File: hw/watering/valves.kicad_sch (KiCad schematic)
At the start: 2 parts, among them J1 Conn_01x02_Pin, U2 AL8860WT

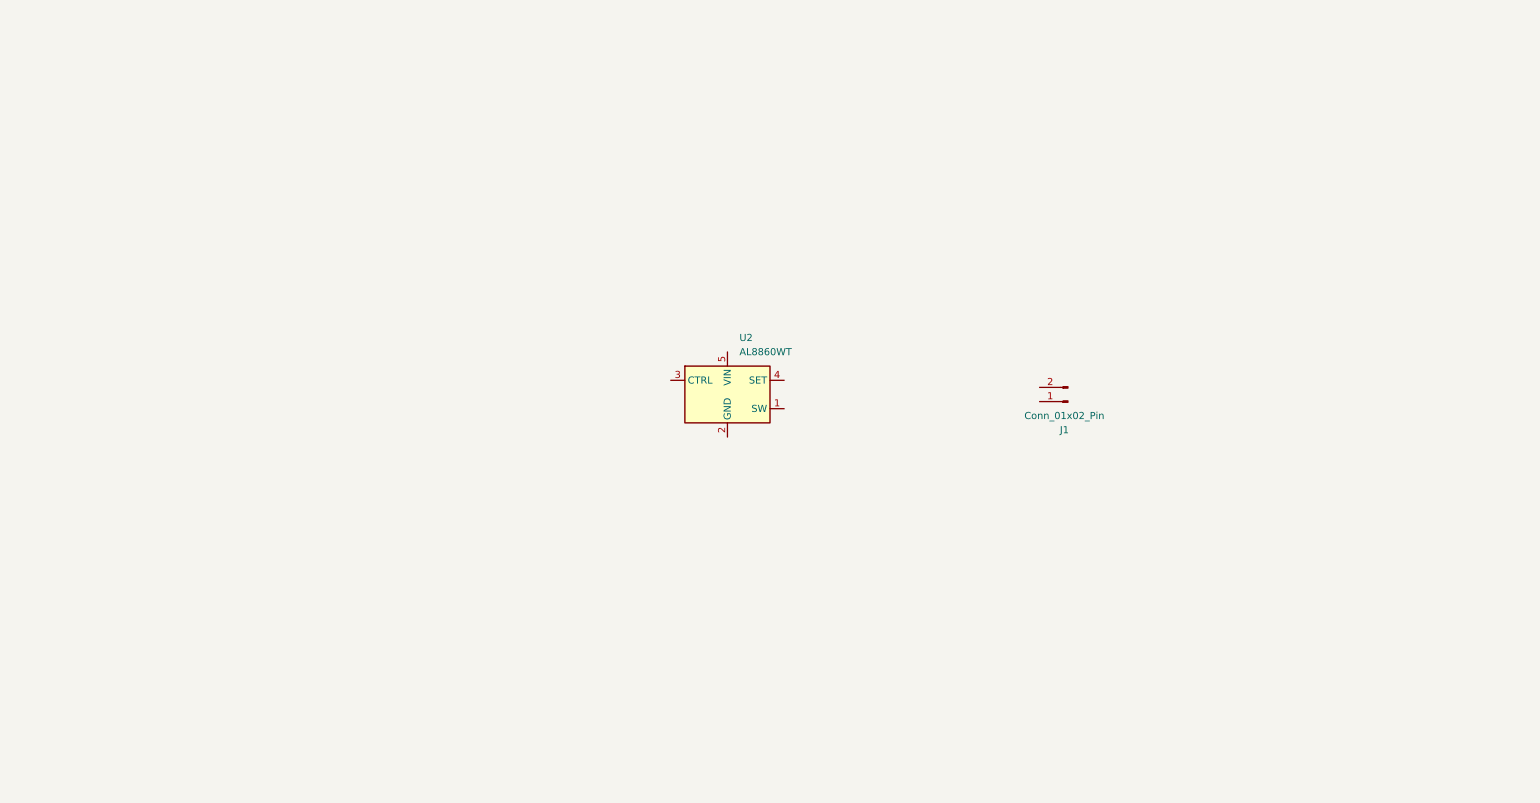
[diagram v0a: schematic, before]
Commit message: added battery management chip
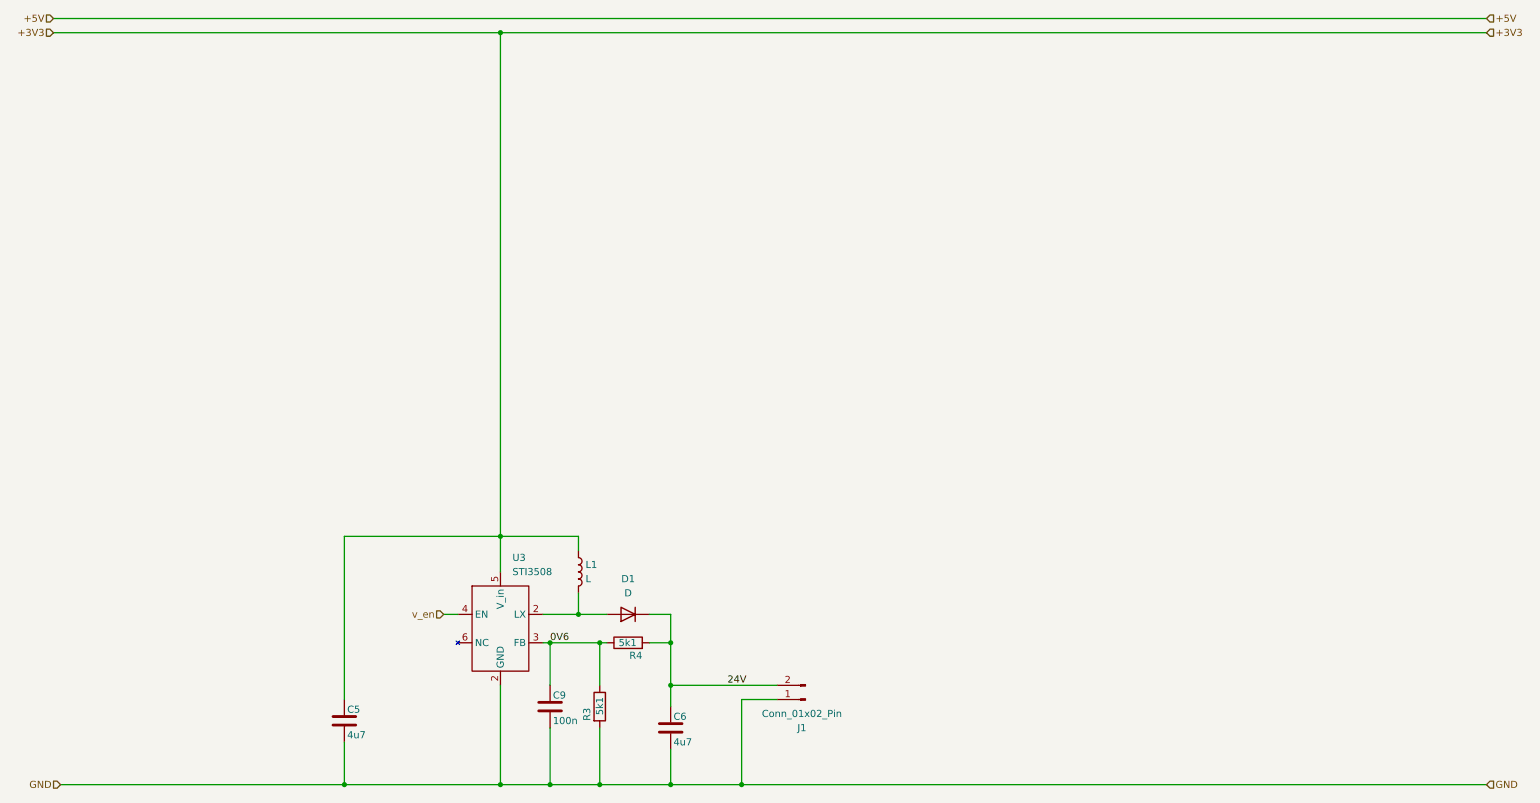
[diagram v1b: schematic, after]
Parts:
- removed U2: AL8860WT, Package_TO_SOT_SMD:TSOT-23-5, symbol Driver_LED:AL8860WT
- added C5, C6: 4u7, Capacitor_SMD:C_0603_1608Metric, symbol Device:C
- added C9: 100n, Capacitor_SMD:C_0603_1608Metric, symbol Device:C
- added D1: D, symbol Device:D
- added L1: L, symbol Device:L
- added R3, R4: 5k1, Resistor_SMD:R_0603_1608Metric, symbol Device:R
- added U3: STI3508, Package_TO_SOT_SMD:SOT-23-6, symbol sti3508:STI3508
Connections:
- net GND: now reaches J1.1 (Pin_1)
- net GND: now also C5.2, C6.2, C9.2, R3.2, U3.2 (LX)
- net 24V: now reaches J1.2 (Pin_2)
- net 24V: now also C6.1, D1.1 (K), R4.2
- new net: D1.2 (A), L1.2, U3.2 (LX)
- new net +3V3: C5.1, L1.1, U3.5 (V_in)
- new net 0V6: C9.1, R3.1, R4.1, U3.3 (FB)
- new net v_en: U3.4 (EN)
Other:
- moved on the sheet: J1

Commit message: updated power
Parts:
- removed C5, C6: 4u7, Capacitor_SMD:C_0603_1608Metric, symbol Device:C
- removed C9: 100n, Capacitor_SMD:C_0603_1608Metric, symbol Device:C
- removed D1: D, symbol Device:D
- removed L1: L, symbol Device:L
- added C29, C33: 22u, Capacitor_SMD:C_1206_3216Metric, symbol Device:C
- added D6: SS210, Diode_SMD:D_SMA, symbol Device:D
- added L5: 22u, Inductor_SMD:L_Wuerth_MAPI-4030, symbol Device:L
- R12: renamed from R3; value 5k1 -> 1k
- R13: renamed from R4; value 5k1 -> 39k
- renumbered J1 to J4, U3 to U6
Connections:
- net +3V3: now also C29.1, L5.1
- net 24V: now also C33.1, D6.1 (K)
- net GND: now also C29.2, C33.2
- new net: D6.2 (A), L5.2, U6.2 (LX)

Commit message: hardware progres
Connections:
- net at D6.2 (A), L5.2: now also U6.1 (LX); no longer U6.2 (LX)
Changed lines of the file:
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@@
 		(pin "3"
 		)
-		(pin "2"
+		(pin "1"
 		)
 		(instances
@@
 			)
 		)
-		(property "Datasheet" ""
+		(property "Datasheet" "https://jlc-prod-smt.oss-eu-central-1.aliyuncs.com/smtDataManualFile/8579706240215273472-C23153.pdf?response-content-disposition=attachment%3B%20filename%3DC23153.pdf%3B%20filename%2A%3DUTF-8%27%27C23153.pdf&x-oss-date=20260604T212837Z&x-oss-expires=1800&x-oss-security-token=CAISgAN1q6Ft5B2yfSjIr5qGBvnBmah58ZCnSW2IvnU%2FOOZNta3duzz2IHhMdHJsAOodtv0%2FmmhT6PkclqRLcbhpcmfjV%2BZHzLB8qc9%2FokVA4J7b16cNrbH4M4H6aXeirtuwDsz9SNTCALjPD3nPii50x5bjaDymRCbLGJaViJlhHLN1Ow6jdmhpCctxLAlvo9NgFxm3D%2Fu2NQPwiWf9FVdhvhEG6Vly8qOi2MaRmFy8yFTx0b0SvJ%2BjYMrmPctoN9JnSdC5mfdzau3a1TJ84gRD0a5wkaVA1zbDs5bfISEIuUzebreLqY03dV4mOvdqIcMe8qigz88fk%2FfIioH6xyxKOexoSCnFTOiiupCcQLPyao9jLu6iayqViY7QaIOTqQohZmkAMwVOasAsI3Ngh4zF97Qt0cVNkXO9gWfLI8DtuMleWqrvQN5iAnSgc5lCkRRYwGs1287ugXlSQzo890KPDAEovaKCnZ2ZSfh7Y4sNknI6i%2Bfc2Se2MIkILjrImKKWD5sagAFp6e2CTF5gXCAetl%2FZznzBeiqXvbdtrNp24XwBckBwOk4pCo9PLwSFMgOtQSf5U6kP%2F%2Bd1fI%2BKr022AwW2hsiCSfA6ItkAjrYqmnkpM1k6ce1E8ls7kKfeT%2Fq%2FikPDk77ij56kdNpXvKHTlexuI%2FHtV9DEGaEJEWVb894cTL2j2iAA&x-oss-signature-version=OSS4-HMAC-SHA256&x-oss-credential=STS.NY3MCutwXFRLKK9Zuj4iaZhvY%2F20260604%2Feu-central-1%2Foss%2Faliyun_v4_request&x-oss-signature=50b712f2b003cbfdc0278338a33b0530e7203f95c21e53b9561c1751bbef5ab5"
 			(at 123.19 133.35 0)
 			(hide yes)
@@
 			)
 		)
-		(property "Description" "Resistor"
+		(property "Description" "C23153"
 			(at 123.19 133.35 0)
 			(hide yes)
@@
 			)
 		)
-		(property "Datasheet" ""
+		(property "Datasheet" "https://jlc-prod-smt.oss-eu-central-1.aliyuncs.com/smtDataManualFile/8579706098724622336-C21190.pdf?response-content-disposition=attachment%3B%20filename%3DC21190.pdf%3B%20filename%2A%3DUTF-8%27%27C21190.pdf&x-oss-date=20260604T201055Z&x-oss-expires=1800&x-oss-security-token=CAISgAN1q6Ft5B2yfSjIr5rnDe%2F5h6h02fGfW1HcsFYmaelfp6rpszz2IHhMdHJsAOodtv0%2FmmhT6PkclqRLcbhpcmfjV%2BZHzLB8qeACnUZA4J7b16cNrbH4M4H6aXeirtuwDsz9SNTCALjPD3nPii50x5bjaDymRCbLGJaViJlhHLN1Ow6jdmhpCctxLAlvo9NgFxm3D%2Fu2NQPwiWf9FVdhvhEG6Vly8qOi2MaRmFy8yFTx0b0SvJ%2BjYMrmPctoN9JnSdC5mfdzau3a1TJ84gRD0a5wkaVA1zbDs5bfISEIuUzebreLqY03dV4mOvdqIcMe8qigz88fk%2FfIioH6xyxKOexoSCnFTOiiupCcQLPyao9jLu6iayqViY7QaIOTqQohZmkAMwVOasAsI3Ngh4zF97Qt0cVNkXO9gWfLI8DtuMleWhqD30JB3tHD0eS19jklBdzSlusJRAJJUVBflCeKEaRNSAd3WGhEfM2%2BBt4QT30w5N2u00S8OSMIc%2BkdiqKWD5sagAFWQNkecW6D1E4coUzPadT7SCc3f42V3X5rSfMFH84ElX%2BTmNGNYscgqDx0xyaTJyyrM%2BFQW4w%2FhWX4qrYQWwgwoGw%2BQzNTMlILHbcsYIbLhGAndRWnhNlBy%2F%2FsrfRbXWVyCjftSb4xwrnr%2BixQsq7hkcXqmYOc23lG%2B0BooZpCuSAA&x-oss-signature-version=OSS4-HMAC-SHA256&x-oss-credential=STS.NYRFUMjwUn3tYwmTVsefsHoBQ%2F20260604%2Feu-central-1%2Foss%2Faliyun_v4_request&x-oss-signature=c8ef4b7bb2f46d5880b5f7d119351002df83d06270cd391a72e44158b7fb7248"
 			(at 118.11 144.78 0)
 			(hide yes)
@@
 			)
 		)
-		(property "Description" "Resistor"
+		(property "Description" "C21190"
 			(at 118.11 144.78 0)
 			(hide yes)

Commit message: routing done
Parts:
- J4: footprint (none) -> DORABO:DB142R-5.08-2P-GN
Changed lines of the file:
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@@
 			)
 		)
-		(property "Footprint" ""
+		(property "Footprint" "DORABO:DB142R-5.08-2P-GN"
 			(at 154.94 143.51 0)
 			(hide yes)
@@
 			)
 		)
-		(property "Datasheet" ""
+		(property "Datasheet" "https://jlc-prod-smt.oss-eu-central-1.aliyuncs.com/smtDataManualFile/8588944103362990080-C2898709.pdf?response-content-disposition=attachment%3B%20filename%3DC2898709.pdf%3B%20filename%2A%3DUTF-8%27%27C2898709.pdf&x-oss-date=20260610T103254Z&x-oss-expires=1800&x-oss-security-token=CAISgAN1q6Ft5B2yfSjIr5rzGerOqIdH2oOoclzHiVFsdbhe1vCYszz2IHhMdHJsAOodtv0%2FmmhT6PkclqRLcbhpcmfjV%2BZHzLB8qdNq3GlC4J7b16cNrbH4M4H6aXeirtuwDsz9SNTCALjPD3nPii50x5bjaDymRCbLGJaViJlhHLN1Ow6jdmhpCctxLAlvo9NgFxm3D%2Fu2NQPwiWf9FVdhvhEG6Vly8qOi2MaRmFy8yFTx0b0SvJ%2BjYMrmPctoN9JnSdC5mfdzau3a1TJ84gRD0a5wkaVA1zbDs5bfISEIuUzebreLqY03dV4mOvdqIcMe8qigz88fk%2FfIioH6xyxKOexoSCnFTOiiupCcQLPyao9jLu6iayqViY7QaIOTqQohZmkAMwVOasAsI3Ngh4zF97Qt0cVNkXO9gWfLI8DtuMleWirs1UNH%2FtHD0eS19jklBdzSlusJRAJJUVBflCeKEaRNSAd3WGhEfM2%2BBt4QT30w5N2u00S8OSMIsaRmZ6KWD5sagAEvGX7RQli9n0idv9ihEU8A%2Bbh5MIwx%2F6mEDEdw7rPt8GvYywCHHAO%2FvmfamD6hWJK1CjyEuU3UmXrstWZ7FJZiXCRquNSQNh07tVtxLzhRH4RSBWWrBck%2B00KmW9tmwnDDBERstBLHwgZAtDcvABP8phEVP1O0gWNEZDZaGHKiVSAA&x-oss-signature-version=OSS4-HMAC-SHA256&x-oss-credential=STS.NYFRPzEXfmACpzvmQ9y7r953Q%2F20260610%2Feu-central-1%2Foss%2Faliyun_v4_request&x-oss-signature=91314ede9ab8009bd2a96ac59210a76d2245a17ff8fcc2e7e63cd5e128038b30"
 			(at 154.94 143.51 0)
 			(hide yes)
@@
 			)
 		)
-		(property "Description" "Generic connector, single row, 01x02, script generated"
+		(property "Description" "C2898709"
 			(at 154.94 143.51 0)
 			(hide yes)

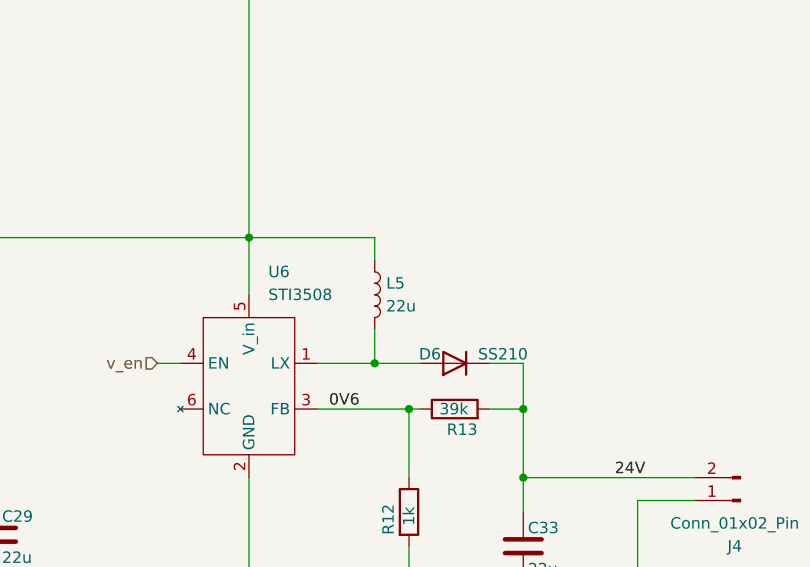
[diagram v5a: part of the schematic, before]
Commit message: updated inductors
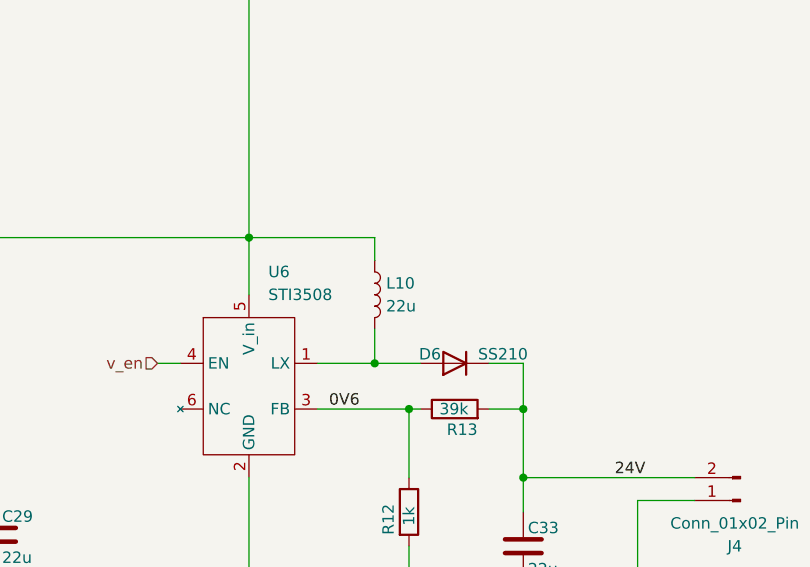
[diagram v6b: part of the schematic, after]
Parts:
- removed L5: 22u, Inductor_SMD:L_Wuerth_MAPI-4030, symbol Device:L
- added L10: 22u, Inductor_SMD:L_Changjiang_FTC303020D, symbol Device:L
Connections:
- net +3V3: now also L10.1
- net at D6.2 (A), U6.1 (LX): now also L10.2
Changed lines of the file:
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@@
+	)
+	(symbol
+		(lib_id "Device:L")
+		(at 114.3 120.65 0)
+		(unit 1)
+		(body_style 1)
+		(exclude_from_sim no)
+		(in_bom yes)
+		(on_board yes)
+		(in_pos_files yes)
+		(dnp no)
+		(fields_autoplaced yes)
+		(property "Reference" "L10"
+			(at 115.57 119.3799 0)
+			(show_name no)
+			(do_not_autoplace no)
+			(effects
+				(font
+					(size 1.27 1.27)
+				)
+				(justify left)
+			)
+		)
+		(property "Value" "22u"
+			(at 115.57 121.9199 0)
+			(show_name no)
+			(do_not_autoplace no)
+			(effects
+				(font
+					(size 1.27 1.27)
+				)
+				(justify left)
+			)
+		)
+		(property "Footprint" "Inductor_SMD:L_Changjiang_FTC303020D"
+			(at 114.3 120.65 0)
+			(hide yes)
+			(show_name no)
+			(do_not_autoplace no)
+			(effects
+				(font
+					(size 1.27 1.27)
+				)
+			)
+		)
+		(property "Datasheet" "https://jlc-prod-smt.oss-eu-central-1.aliyuncs.com/smtDataManualFile/8603011017442553856-C18724424.pdf?response-content-disposition=attachment%3B%20filename%3DC18724424.pdf%3B%20filename%2A%3DUTF-8%27%27C18724424.pdf&x-oss-date=20260615T131049Z&x-oss-expires=1800&x-oss-security-token=CAISgAN1q6Ft5B2yfSjIr5r7EvjHqrJS76GJWlCDrFA3esRehaLlqTz2IHhMdHJsAOodtv0%2FmmhT6PkclqRLcbhpcmfjV%2BZHzLB8qbYvhD9F4J7b16cNrbH4M4H6aXeirtuwDsz9SNTCALjPD3nPii50x5bjaDymRCbLGJaViJlhHLN1Ow6jdmhpCctxLAlvo9NgFxm3D%2Fu2NQPwiWf9FVdhvhEG6Vly8qOi2MaRmFy8yFTx0b0SvJ%2BjYMrmPctoN9JnSdC5mfdzau3a1TJ84gRD0a5wkaVA1zbDs5bfISEIuUzebreLqY03dV4mOvdqIcMe8qigz88fk%2FfIioH6xyxKOexoSCnFTOiiupCcQLPyao9jLu6iayqViY7QaIOTqQohZmkAMwVOasAsI3Ngh4zF97Qt0cVNkXO9gWfLI8DtuMleWkqmQftNonSgc5lCkRRYwGs1287ugXlSQzo890KPDAEovaKCnZ2ZSfh7Y4sNknI6i%2Bfc2Se2MIkI78F9wqKWD5sagAGgIrBpqkaDNLB%2FeRrJRXX%2BUI0WHkJQELKIEfuONtPHcqXYkRDIHor0h8sEmAzdWEcuJqyAotIM3sYVhSK9RCw9rtluv0dJx48JCxsibZlIjb%2B0NEIprmvzFpJBKJEQoS2JBuBmZ0uKENGbbnHMTewPmke4yqImGUR1dELAyCJ5ASAA&x-oss-signature-version=OSS4-HMAC-SHA256&x-oss-credential=STS.NYNYBsGmsXcbXv2HPbvKrjgNK%2F20260615%2Feu-central-1%2Foss%2Faliyun_v4_request&x-oss-signature=9cbeeebf1f2dbb1e5d82ef5fe3da511c573dfc2eaeab7f382c23f43e5666c8af"
+			(at 114.3 120.65 0)
+			(hide yes)
+			(show_name no)
+			(do_not_autoplace no)
+			(effects
+				(font
+					(size 1.27 1.27)
+				)
+			)
+		)
+		(property "Description" "C18724424"
+			(at 114.3 120.65 0)
+			(hide yes)
+			(show_name no)
+			(do_not_autoplace no)
+			(effects
+				(font
+					(size 1.27 1.27)
+				)
+			)
+		)
+		(pin "2"
+		)
+		(pin "1"
+		)
+		(instances
+			(project "watering"
+				(path "/cfeeaa6f-be25-403f-b03c-39be367d5a74/618729c2-2044-4b2a-920d-2470c2d6b979"
+					(reference "L11")
+					(unit 1)
+				)
+				(path "/cfeeaa6f-be25-403f-b03c-39be367d5a74/7dcde84c-c5b2-4a67-a087-35c6c8d4203a"
+					(reference "L10")
+					(unit 1)
+				)
+			)
+		)
 	)
 	(symbol
@@
 					(unit 1)
 				)
-			)
-		)
-	)
-	(symbol
-		(lib_id "Device:L")
-		(at 114.3 120.65 0)
-		(unit 1)
-		(body_style 1)
-		(exclude_from_sim no)
-		(in_bom yes)
-		(on_board yes)
-		(in_pos_files yes)
-		(dnp no)
-		(fields_autoplaced yes)
-		(property "Reference" "L5"
-			(at 115.57 119.3799 0)
-			(show_name no)
-			(do_not_autoplace no)
-			(effects
-				(font
-					(size 1.27 1.27)
-				)
-				(justify left)
-			)
-		)
-		(property "Value" "22u"
-			(at 115.57 121.9199 0)
-			(show_name no)
-			(do_not_autoplace no)
-			(effects
-				(font
-					(size 1.27 1.27)
-				)
-				(justify left)
-			)
-		)
-		(property "Footprint" "Inductor_SMD:L_Wuerth_MAPI-4030"
-			(at 114.3 120.65 0)
-			(hide yes)
-			(show_name no)
-			(do_not_autoplace no)
-			(effects
-				(font
-					(size 1.27 1.27)
-				)
-			)
-		)
-		(property "Datasheet" "https://jlc-prod-smt.oss-eu-central-1.aliyuncs.com/smtDataManualFile/8588905405544615936-C843299.pdf?response-content-disposition=attachment%3B%20filename%3DC843299.pdf%3B%20filename%2A%3DUTF-8%27%27C843299.pdf&x-oss-date=20260604T164541Z&x-oss-expires=3600&x-oss-security-token=CAISgAN1q6Ft5B2yfSjIr5mCEsvdgJF2x5SRVR%2BDlG9hdOdDiq3Z0zz2IHhMdHJsAOodtv0%2FmmhT6PkclqRLcbhpcmfjV%2BZHzLB8qYg%2Fsn1A4J7b16cNrbH4M4H6aXeirtuwDsz9SNTCALjPD3nPii50x5bjaDymRCbLGJaViJlhHLN1Ow6jdmhpCctxLAlvo9NgFxm3D%2Fu2NQPwiWf9FVdhvhEG6Vly8qOi2MaRmFy8yFTx0b0SvJ%2BjYMrmPctoN9JnSdC5mfdzau3a1TJ84gRD0a5wkaVA1zbDs5bfISEIuUzebreLqY03dV4mOvdqIcMe8qigz88fk%2FfIioH6xyxKOexoSCnFTOiiupCcQLPyao9jLu6iayqViY7QaIOTqQohZmkAMwVOasAsI3Ngh4zF97Qt0cVNkXO9gWfLI8DtuMleWoqhAFRO3tHD0eS19jklBdzSlusJRAJJUVBflCeKEaRNSAd3WGhEfM2%2BBt4QT30w5N2u00S8OSMIKT4xNqKWD5sagAFjpi0uueLITfuvBAmsnLaeVepWlRfyWJVQZNGhbataE8ReXt3OOchcwgtji5Ai2iONRYSv7hixir4FvwLOSwdcmetKzf2kYykoq7HUJ%2BOUGjjEEmtElKvPa2TG2TAmg05P9aIeO9iCDss8eOTjWFw5kKj4hGJtb%2Fto4b8kIVkQDiAA&x-oss-signature-version=OSS4-HMAC-SHA256&x-oss-credential=STS.NZ7YqimNWpVzW92po4xhoehr1%2F20260604%2Feu-central-1%2Foss%2Faliyun_v4_request&x-oss-signature=0f12ab1dbea620ad72922b29a9cc5c1da75e3d079b537053c1bc3edf0f1800e3"
-			(at 114.3 120.65 0)
-			(hide yes)
-			(show_name no)
-			(do_not_autoplace no)
-			(effects
-				(font
-					(size 1.27 1.27)
-				)
-			)
-		)
-		(property "Description" "C843299"
-			(at 114.3 120.65 0)
-			(hide yes)
-			(show_name no)
-			(do_not_autoplace no)
-			(effects
-				(font
-					(size 1.27 1.27)
-				)
-			)
-		)
-		(pin "2"
-		)
-		(pin "1"
-		)
-		(instances
-			(project "watering"
-				(path "/cfeeaa6f-be25-403f-b03c-39be367d5a74/618729c2-2044-4b2a-920d-2470c2d6b979"
-					(reference "L6")
-					(unit 1)
-				)
-				(path "/cfeeaa6f-be25-403f-b03c-39be367d5a74/7dcde84c-c5b2-4a67-a087-35c6c8d4203a"
-					(reference "L5")
-					(unit 1)
-				)
